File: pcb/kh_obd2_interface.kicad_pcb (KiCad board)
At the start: 2 copper layers, 60 x 50 mm, 50 parts, among them J1 OBD2, J2 CAN, J3 USB-C 2.0, J4 RTC_BAT, M1 MountingHole_3.2mm_M3_Pad_Top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, Q201 CSD18540Q5B, SW2 SW_SPDT, U1 STM32G0B1RET6, U2 TLIN2027-Q1, U201 LM74500-Q1, U202 TVS2700DRV, U3 TPSM33620S5QRDNRQ1, U301 TCAN3403-Q1, U302 74LVC1G07, U303 SN74LV1T34DBV, U4 LM1117-Q1-3.3

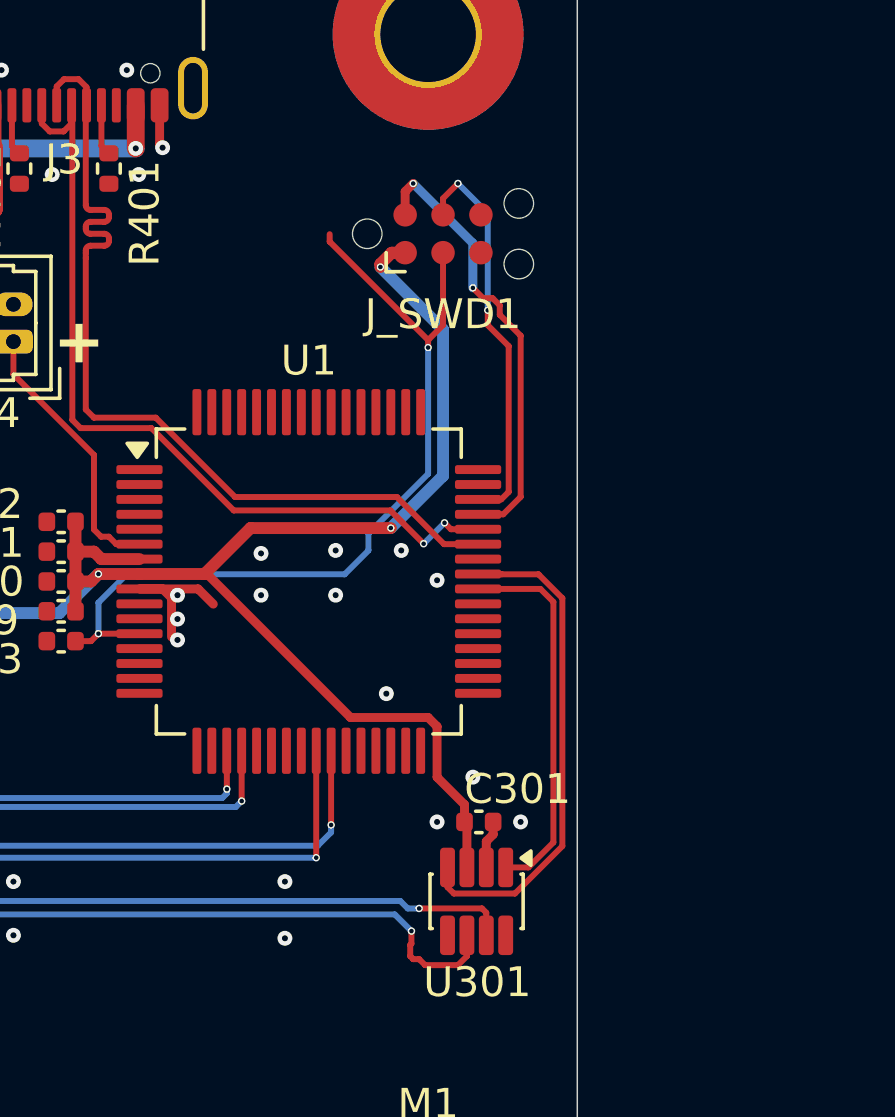
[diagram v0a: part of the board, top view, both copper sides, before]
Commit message: fix CAN tx/rx/stb, remove unused SWO
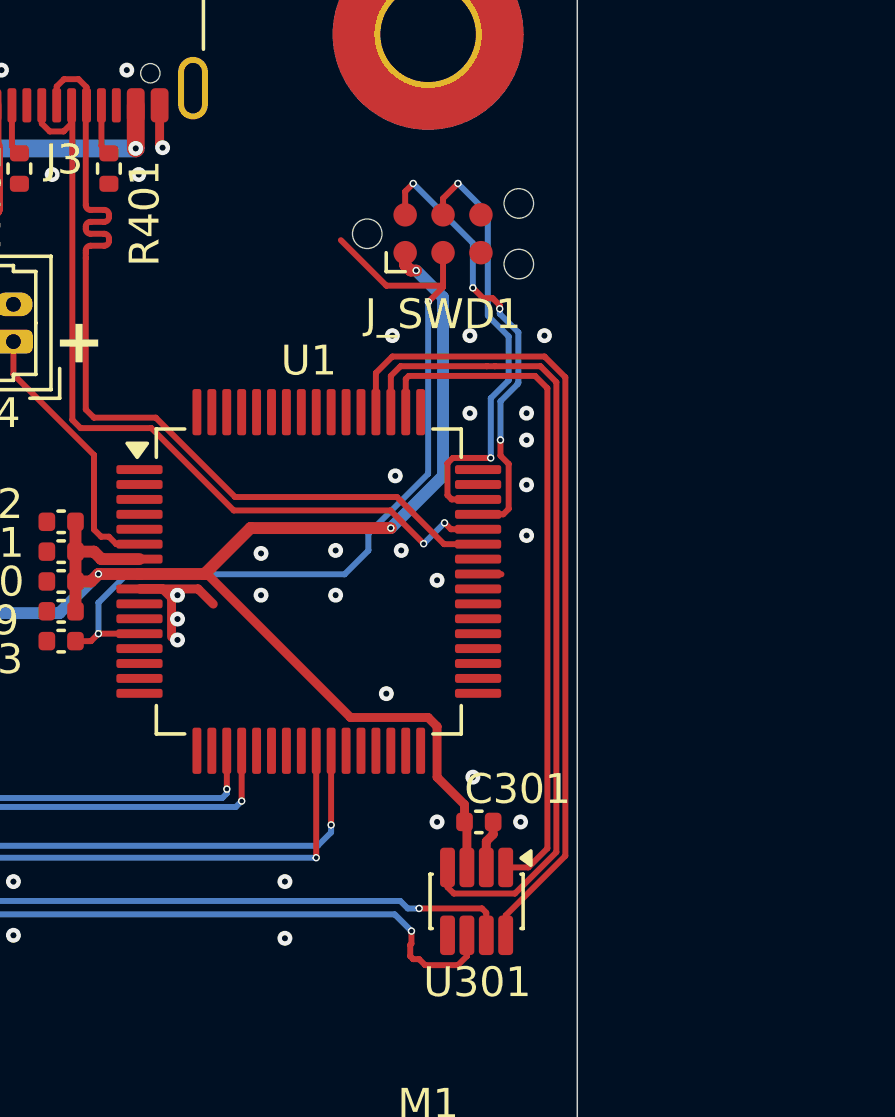
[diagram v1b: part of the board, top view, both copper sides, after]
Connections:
- J_SWD1 pad 6: /Connectors/MCU_SWO -> unconnected-(J_SWD1-Pad6)
- U1 pad 13: unconnected-(U1-PC0-Pad13) -> /MCU/MCU_STATUS_LED
- U1 pad 40: /Communications/TX -> unconnected-(U1-PD8-Pad40)
- U1 pad 41: /Communications/RX -> unconnected-(U1-PD9-Pad41)
- U1 pad 50: unconnected-(U1-PD0-Pad50) -> /Communications/TX
- U1 pad 51: unconnected-(U1-PD1-Pad51) -> /Communications/RX
- U1 pad 52: unconnected-(U1-PD2-Pad52) -> /Communications/STB
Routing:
- net /Communications/STB: track 0.00 -> 27.7 mm
- net /Communications/RX: track 16.7 -> 27.8 mm
- net /Communications/TX: track 12.7 -> 23.2 mm
- net /Connectors/MCU_SWCLK_BOOT0: track 13.4 -> 15.1 mm
- net /Connectors/MCU_NRST: track 29.0 -> 28.1 mm
- net +3V3: track 104.4 -> 103.6 mm
- net /Connectors/MCU_SWDIO: track 15.0 -> 15.2 mm, vias 2 -> 4
- net GND: vias 141 -> 150

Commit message: moved EVERYTHING
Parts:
- moved J4 30.1 mm to (38.1, 52.3), turned to 0 degrees
- moved C301 6.70 mm to (67.5, 46.9)
- moved C10 6.70 mm to (53.5, 38.9)
- moved C11 6.70 mm to (53.5, 37.9)
- moved C12 6.70 mm to (53.5, 36.9)
- moved C13 6.70 mm to (53.5, 40.9)
- moved C9 6.70 mm to (53.5, 39.9)
- moved U1 6.70 mm to (61.8, 38.9)
- moved U301 6.70 mm to (67.5, 49.6)
- moved J_SWD1 0.06 mm to (73.0, 26.6)
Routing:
- net /Connectors/RTC_VBAT: track 9.35 -> 37.5 mm, vias 0 -> 2
- net /MCU/MCU_STATUS_LED: track 0.00 -> 21.2 mm
- net /Communications/RX: track 27.8 -> 17.5 mm, vias 0 -> 2
- net /Communications/KLINE.RX: track 28.9 -> 21.1 mm
- net /Communications/KLINE.TX: track 27.6 -> 20.2 mm
- net /Communications/STB: track 27.7 -> 20.7 mm, vias 0 -> 2
- net /Communications/CAN.P: track 55.9 -> 49.5 mm
- net /Communications/HLINE.RX: track 30.4 -> 23.9 mm
- net /Communications/HLINE.TX: track 37.7 -> 31.3 mm
- net /Communications/CAN.N: track 54.2 -> 47.8 mm
- net /Connectors/MCU_NRST: track 28.1 -> 32.3 mm, vias 2 -> 4
- net /Communications/TX: track 23.2 -> 19.3 mm, vias 0 -> 2
- net /Connectors/MCU_SWCLK_BOOT0: track 15.1 -> 17.5 mm
- net /Connectors/DN: track 30.2 -> 31.8 mm
- net /Connectors/MCU_SWDIO: track 15.2 -> 16.7 mm, vias 4 -> 2
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- added copper zone on F.Cu, net +3V3

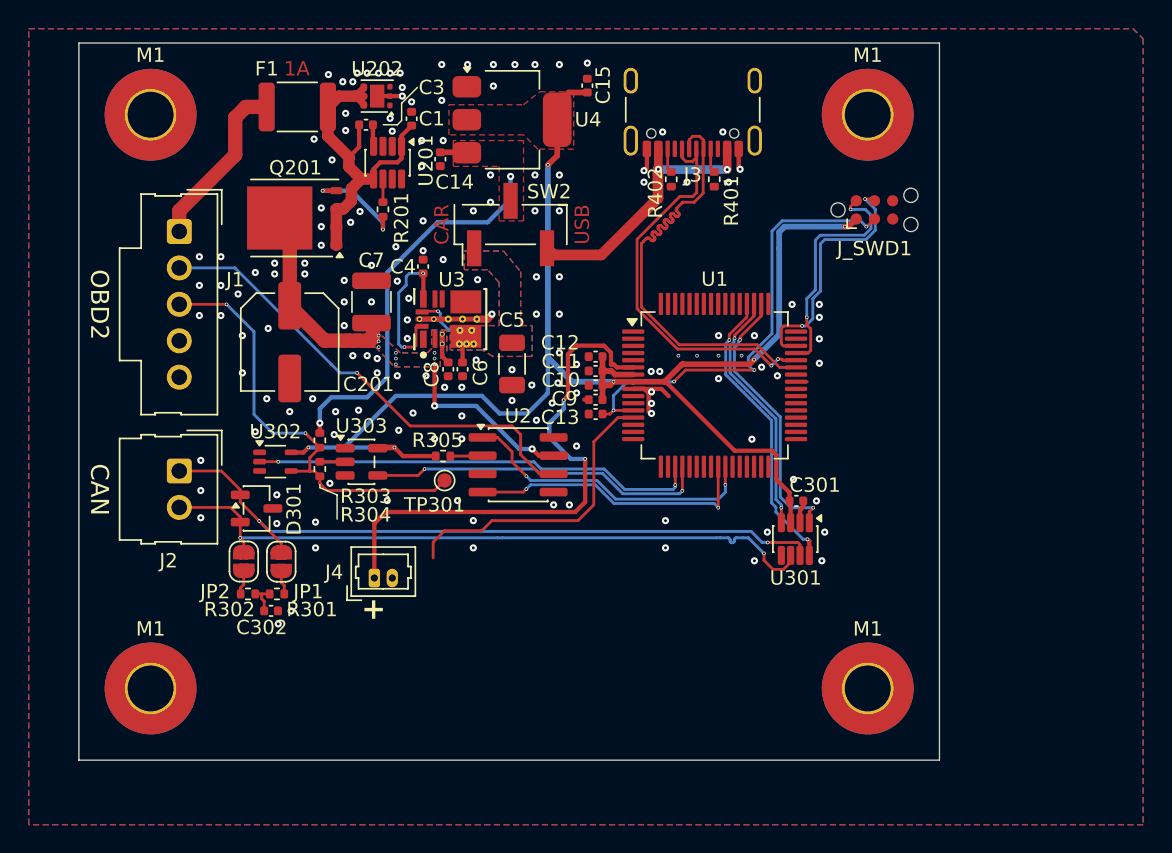
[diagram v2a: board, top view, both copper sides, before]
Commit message: status/info leds, extra 5v cap
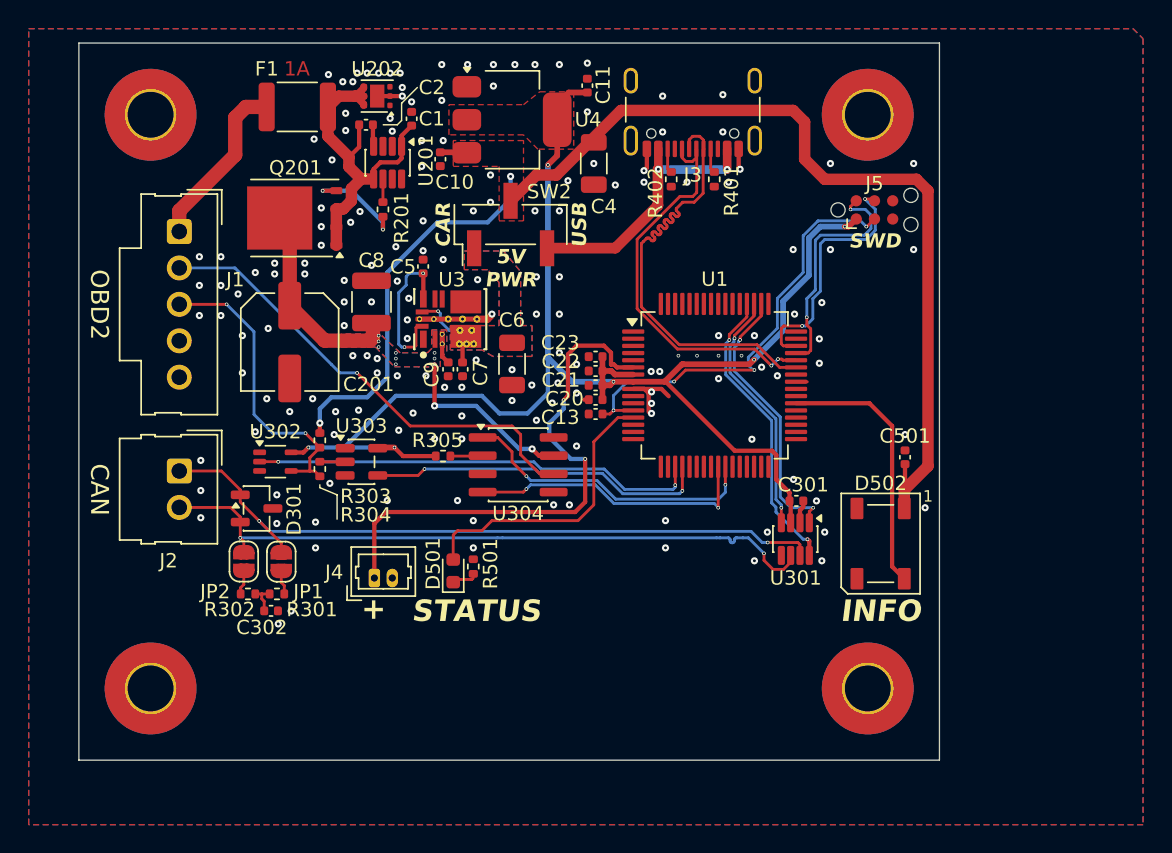
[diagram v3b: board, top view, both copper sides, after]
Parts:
- removed TP301: HLine, TestPoint:TestPoint_Pad_D1.0mm
- added C4: 47uF, Capacitor_SMD:C_1206_3216Metric, F.Cu at (53.4, 23.4)
- added C501: 100nF, Capacitor_SMD:C_0402_1005Metric, F.Cu at (75.1, 43.9)
- added D501: LED, LED_SMD:LED_0603_1608Metric, F.Cu at (43.6, 51.8)
- added D502: INFO_LED, LED_SMD:LED_WS2812B_PLCC4_5.0x5.0mm_P3.2mm, F.Cu at (73.4, 49.9)
- added R501: 600R, Resistor_SMD:R_0402_1005Metric, F.Cu at (45.0, 51.5)
- renumbered C14 to C10, C15 to C11, C3 to C2, C9 to C20, C10 to C21, C11 to C22, C12 to C23, C4 to C5, C5 to C6, C6 to C7, C7 to C8, C8 to C9, J_SWD1 to J5, U2 to U304
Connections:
- U1 pad 13: /MCU/MCU_STATUS_LED -> /HMI/MCU_STATUS_LED
- U1 pad 38: unconnected-(U1-PC6-Pad38) -> /HMI/MCU_LED_DRV
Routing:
- net +5V: track 28.7 -> 90.2 mm
- net /MCU/MCU_STATUS_LED: track 21.2 -> 0.00 mm
- net /HMI/MCU_STATUS_LED: track 0.00 -> 20.2 mm
- net /HMI/MCU_LED_DRV: track 0.00 -> 18.4 mm
- net /Connectors/H Line: track 31.1 -> 21.4 mm
- net Net-(D501-K): track 0.00 -> 1.52 mm
- net /Connectors/MCU_NRST: track 32.3 -> 30.8 mm
- net +3V3: track 103.2 -> 101.8 mm
- net GND: vias 157 -> 167
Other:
- board text added: "5V PWR"
- board text added: "INFO"
- board text added: "STATUS"
- board text added: "SWD"

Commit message: dbg uart, nrst, SCS drive, etc
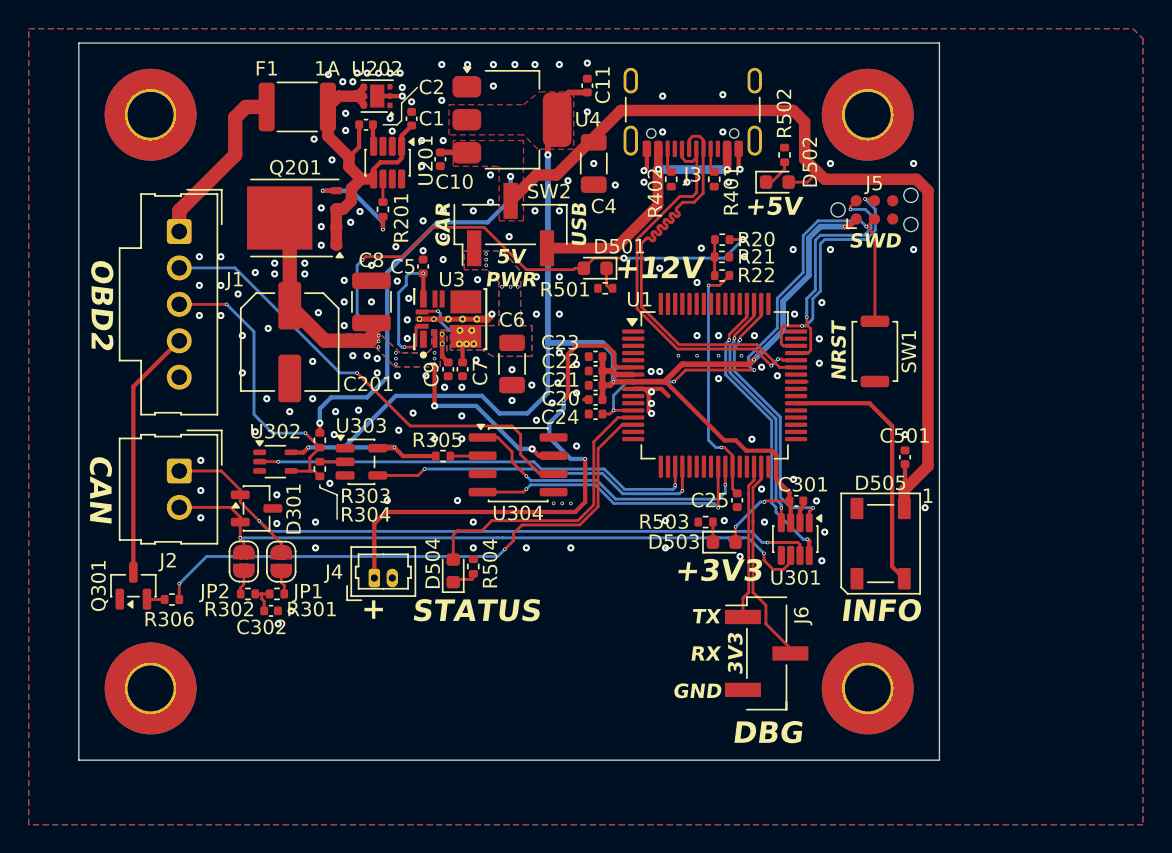
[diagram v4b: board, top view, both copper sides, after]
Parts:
- added C25: 10nF, Capacitor_SMD:C_0402_1005Metric, F.Cu at (63.4, 46.9)
- added D501: LED, LED_SMD:LED_0603_1608Metric, F.Cu at (53.5, 30.7)
- added D502: LED, LED_SMD:LED_0603_1608Metric, F.Cu at (66.2, 24.7)
- added D503: LED, LED_SMD:LED_0603_1608Metric, F.Cu at (62.5, 49.8)
- added J6: Conn_01x03_Pin, Connector_PinHeader_2.54mm:PinHeader_1x03_P2.54mm_Vertical_SMD_Pin1Left, F.Cu at (65.5, 57.6)
- added Q301: 2N3904, Package_TO_SOT_SMD:SOT-23, F.Cu at (21.3, 52.8)
- added R20: 280k, Resistor_SMD:R_0402_1005Metric, F.Cu at (62.4, 28.7)
- added R21: 40.2k, Resistor_SMD:R_0402_1005Metric, F.Cu at (62.3, 29.9)
- added R22: 100r, Resistor_SMD:R_0402_1005Metric, F.Cu at (62.3, 31.2)
- added R306: 1k, Resistor_SMD:R_0402_1005Metric, F.Cu at (24.0, 53.8)
- added R501: 27k, Resistor_SMD:R_0402_1005Metric, F.Cu at (54.2, 32.1)
- added R502: 6.2k, Resistor_SMD:R_0402_1005Metric, F.Cu at (66.7, 22.8)
- added R503: 2.4k, Resistor_SMD:R_0402_1005Metric, F.Cu at (61.2, 48.4)
- added SW1: NRST, Button_Switch_SMD:SW_Push_SPST_NO_Alps_SKRK, F.Cu at (73.0, 36.5)
- renumbered C13 to C24, D501 to D504, D502 to D505, R501 to R504
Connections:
- U1 pad 14: unconnected-(U1-PC1-Pad14) -> /Communications/MCU_SCS_DRIVE
- U1 pad 27: unconnected-(U1-PB0-Pad27) -> /MCU/12V_MEAS
- U1 pad 30: /MCU/DBG_UART.TX -> /Connectors/DBG.TX
- U1 pad 31: /MCU/DBG_UART.RX -> /Connectors/DBG.RX
- U1 pad 62: unconnected-(U1-PB8-Pad62) -> /MCU/MCU_I2C.SCL
- U1 pad 63: unconnected-(U1-PB9-Pad63) -> /MCU/MCU_I2C.SDA
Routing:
- net /Communications/MCU_SCS_DRIVE: track 0.00 -> 40.1 mm, vias 0 -> 2
- net +12V: track 28.5 -> 65.1 mm, vias 11 -> 14
- net /Connectors/SCS: track 0.00 -> 17.5 mm
- net /MCU/12V_MEAS: track 0.00 -> 17.4 mm, vias 0 -> 2
- net /Connectors/DBG.RX: track 0.00 -> 14.3 mm
- net /Connectors/DBG.TX: track 0.00 -> 10.8 mm
- net +3V3: track 101.8 -> 108.9 mm, vias 6 -> 8
- net /Connectors/MCU_NRST: track 30.8 -> 37.7 mm
- net Net-(R20-Pad2): track 0.00 -> 2.47 mm
- net +5V: track 90.2 -> 92.5 mm
- net Net-(D502-K): track 0.00 -> 2.15 mm
- net Net-(D501-K): track 0.00 -> 1.70 mm
- net Net-(D503-K): track 0.00 -> 1.40 mm
- net Net-(Q301-B): track 0.00 -> 1.21 mm
- net GND: vias 167 -> 182
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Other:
- board text added: "+12V"
- board text added: "+3V3"
- board text added: "+5V"
- board text added: "3V3"
- board text added: "DBG"
- board text added: "GND"
- board text added: "RX"
- board text added: "TX"

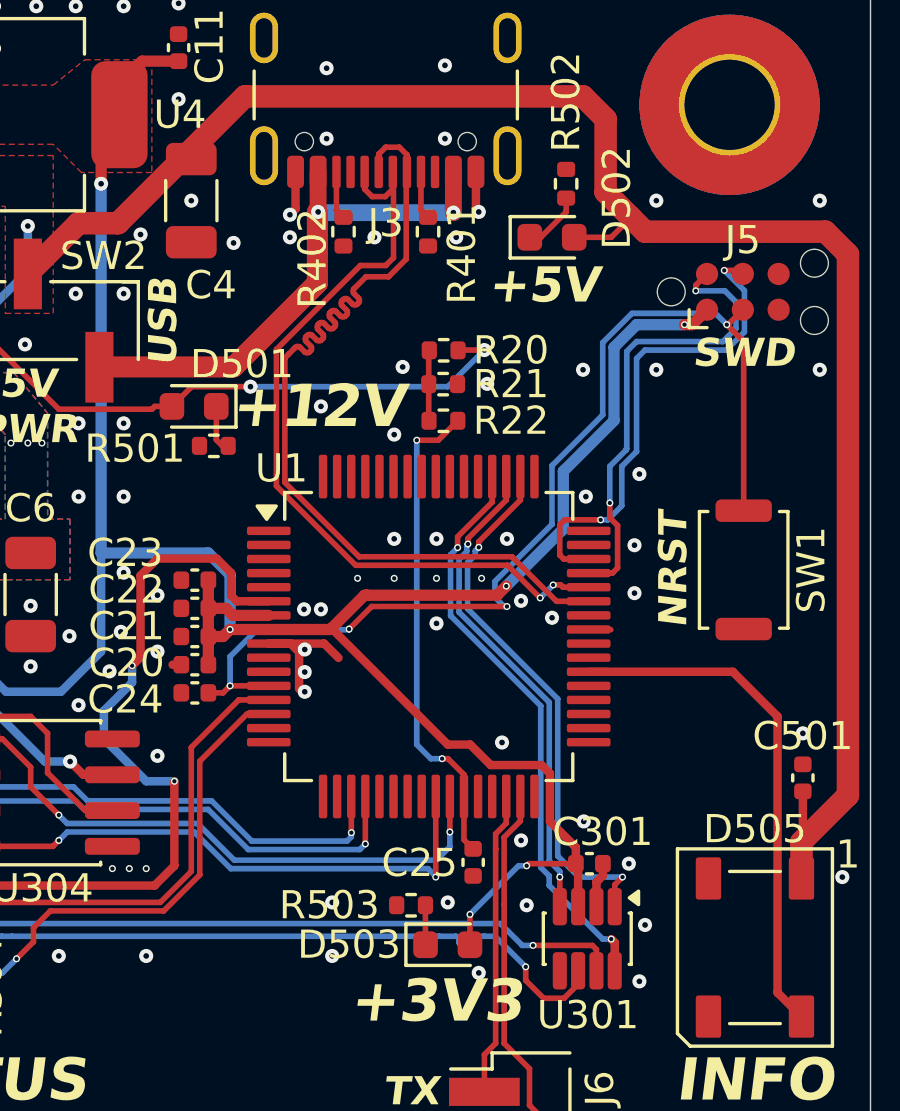
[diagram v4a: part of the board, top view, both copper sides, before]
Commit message: USB reroute
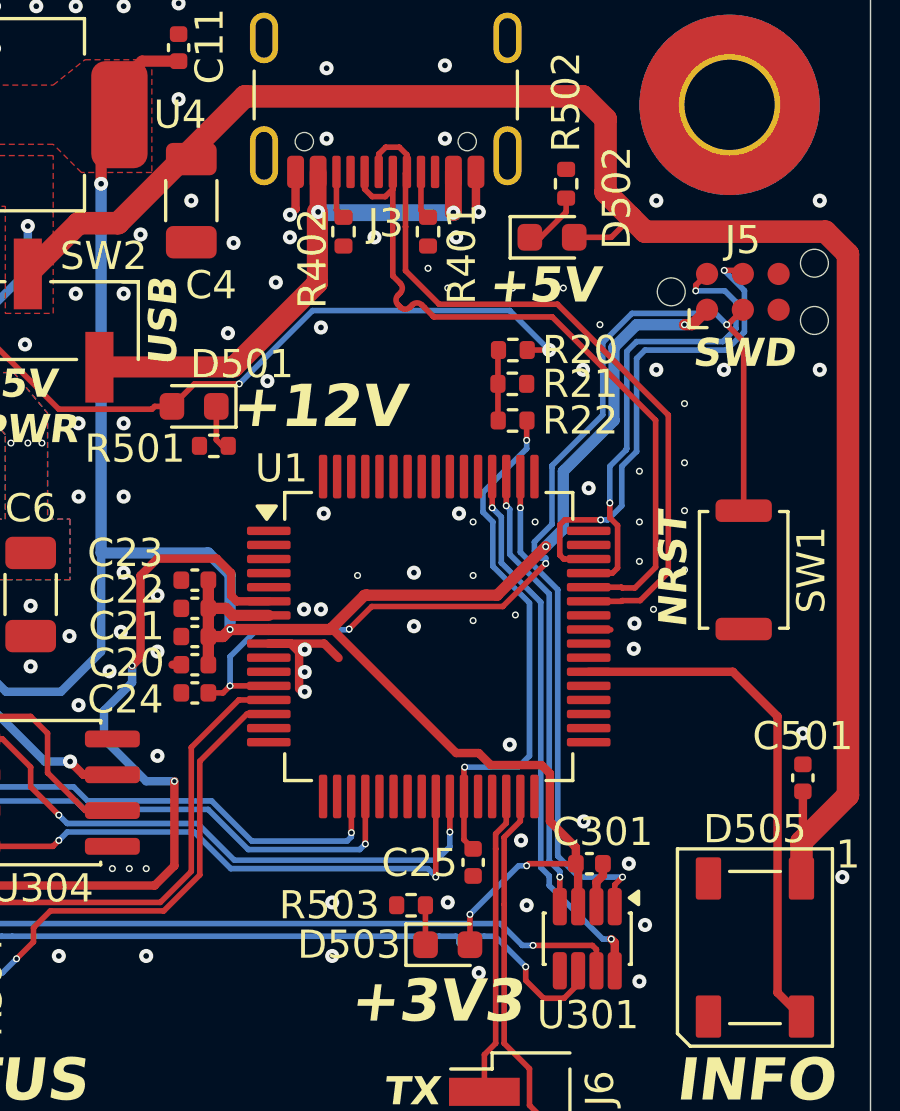
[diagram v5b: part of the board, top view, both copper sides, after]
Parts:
- moved R20 2.45 mm to (64.8, 28.7)
- moved R21 2.45 mm to (64.8, 29.9)
- moved R22 2.45 mm to (64.8, 31.2)
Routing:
- net /Connectors/DN: track 31.8 -> 26.3 mm
- net +12V: track 65.1 -> 68.4 mm
- net /Connectors/DP: track 28.8 -> 26.3 mm, vias 2 -> 0
- net /Communications/TX: track 19.3 -> 17.8 mm
- net /Communications/RX: track 17.5 -> 16.0 mm
- net /MCU/12V_MEAS: track 17.4 -> 18.7 mm
- net /Communications/STB: track 20.7 -> 19.5 mm
- net GND: vias 182 -> 195
